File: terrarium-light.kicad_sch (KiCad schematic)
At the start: 37 parts, among them J1 USB_C_Receptacle_USB2.0_14P, Q1 UMH3N, U1 CH340C, U2 AL8860WT, U3 AL8860WT

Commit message: updates
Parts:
- removed C1, C2: C, symbol Device:C
- removed D13, D14: LED, symbol Device:LED
- removed D25, D26: D, symbol Device:D
- removed L1, L2: L, symbol Device:L
- removed R1, R2: R, symbol Device:R
- removed U2, U3: AL8860WT, Package_TO_SOT_SMD:TSOT-23-5, symbol Driver_LED:AL8860WT
- added C1, C3: C in, symbol Device:C_Small
- added C2, C4: C out, symbol Device:C_Small
- added D13, D14: D_Schottky, symbol Device:D_Schottky
- added D25, D26: LED, symbol Device:LED
- added L1, L2: L_Iron, symbol Device:L_Iron
- added R1, R2: Rset, symbol Device:R_Small
- added U2, U3: TPS61169DCKR, DCK0005A_N, symbol TPS61169DCKR:TPS61169DCKR
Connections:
- net +5V: now also C1.1, C3.1, L1.1, L2.1, U2.5 (VIN), U3.5 (VIN)
- net Earth: now also C1.2, C2.2, C3.2, C4.2, R1.2, R2.2, U2.2 (GND), U3.2 (GND)
- net at D12.1 (K): now also R1.1, U2.3 (FB)
- net at D24.1 (K): now also D25.2 (A)
- net at D1.2 (A): now also C4.1, D13.1 (K)
- net at D15.2 (A): now also C2.1, D14.1 (K)
- new net: D14.2 (A), L2.2, U3.1 (SW)
- new net: D26.1 (K), R2.1, U3.3 (FB)
- new net: D25.1 (K), D26.2 (A)
- new net: D13.2 (A), L1.2, U2.1 (SW)
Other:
- moved on the sheet: D1, D10, D11, D12, D2, D3, D4, D5, D6, D7, D8, D9

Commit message: CH340C seems good
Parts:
- added C5: 0.1uF, symbol Device:C_Small
- added R3, R4: 5.1K, symbol Device:R_Small
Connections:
- net +5V: now also J1.A4 (VBUS), J1.A9 (VBUS), J1.B4 (VBUS), J1.B9 (VBUS), U1.16 (VCC)
- net GND: now also C5.1, R3.2, R4.2
- net at U1.4 (V3): now also C5.2
- net at J1.A5 (CC1): now also R3.1
- net at J1.B5 (CC2): now also R4.1
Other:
- moved on the sheet: J1, Q1A, Q1B, U1

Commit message: updates
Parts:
- added C6: 0.1uF, symbol Device:C_Small
- added C7: 1uF, symbol Device:C_Small
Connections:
- net +5V: no longer U1.16 (VCC)
- net GND: now also C5.2, C6.1, C7.2; no longer C5.1
- net ~{RTS}: no longer Q1.6 (C1)
- net +3.3V: now reaches U1.4 (V3)
- net +3.3V: now also C5.1, U1.16 (VCC), C6.2; no longer C5.2
- net IO0 renamed ESP_IO0
- net ESP_IO0: now also C7.1
- new net ESP_EN: Q1.6 (C1)
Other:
- moved on the sheet: C5, Q1A, Q1B, U1

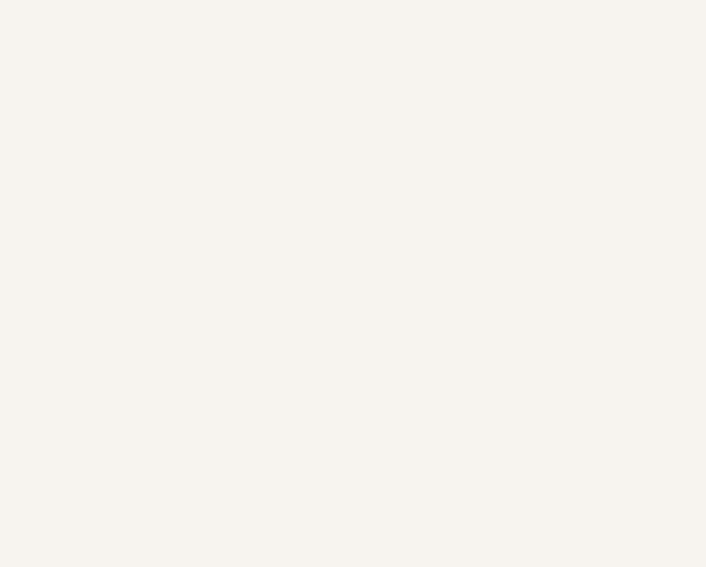
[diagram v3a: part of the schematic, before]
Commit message: what
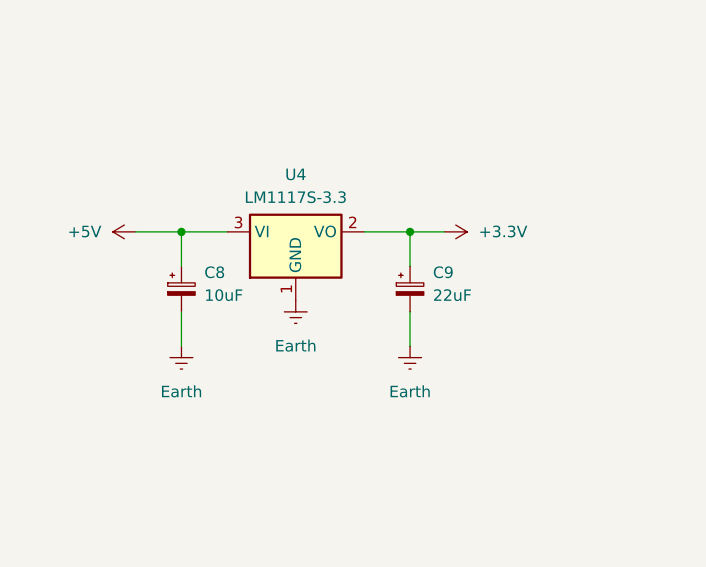
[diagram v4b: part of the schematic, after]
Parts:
- added C8: 10uF, symbol Device:C_Polarized_Small
- added C9: 22uF, symbol Device:C_Polarized_Small
- added U4: LM1117S-3.3, Package_TO_SOT_SMD:TO-263-3_TabPin2, symbol Regulator_Linear:LM1117S-3.3
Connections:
- net +3.3V: now also C9.1, U4.2 (VO)
- net +5V: now also C8.1, U4.3 (VI)
- net Earth: now also C8.2, C9.2, U4.1 (GND)

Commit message: added footprint
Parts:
- added U5: ESP32-S3-MINI-1U, RF_Module:ESP32-S2-MINI-1U, symbol MCU_Espressif:ESP32-S3-MINI-1U
- D1, D10, D11, D12, D15, D16, D17, D18, D19, D2, D20, D21, D22, D23, D24, D25, D26, D3, D4, D5, D6, D7, D8, D9: footprint (none) -> LED_SMD:LED_SPMWHD32AMH0XAR0PR
- J1: footprint (none) -> Connector_USB:USB_C_Receptacle_GCT_USB4105-xx-A_16P_TopMnt_Horizontal
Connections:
- new net: U5.1 (GND), U5.2 (GND), U5.42 (GND), U5.43 (GND), U5.46 (GND), U5.47 (GND), U5.48 (GND), U5.49 (GND), U5.50 (GND), U5.51 (GND), U5.52 (GND), U5.53 (GND), U5.54 (GND), U5.55 (GND), U5.56 (GND), U5.57 (GND), U5.58 (GND), U5.59 (GND), U5.60 (GND), U5.61 (GND), U5.62 (GND), U5.63 (GND), U5.64 (GND), U5.65 (GND)

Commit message: tried to add some stuff
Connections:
- net +3.3V: now also U5.3 (3V3)
- net ESP_EN: now also U5.45 (EN)
- net ESP_IO0: now also U5.4 (IO0)
- net GND: now also U5.1 (GND), U5.2 (GND), U5.42 (GND), U5.43 (GND), U5.46 (GND), U5.47 (GND), U5.48 (GND), U5.49 (GND), U5.50 (GND), U5.51 (GND), U5.52 (GND), U5.53 (GND), U5.54 (GND), U5.55 (GND), U5.56 (GND), U5.57 (GND), U5.58 (GND), U5.59 (GND), U5.60 (GND), U5.61 (GND), U5.62 (GND), U5.63 (GND), U5.64 (GND), U5.65 (GND)
- net ESP_32_RX: now reaches U1.2 (TXD)
- net ESP_32_RX: now also U5.40 (RXD0)
- net ESP_32_TX: now reaches U1.3 (RXD)
- net ESP_32_TX: now also U5.39 (TXD0)
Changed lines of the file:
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@@
 	(wire
 		(pts
+			(xy 30.48 59.69) (xy 40.64 59.69)
+		)
+		(stroke
+			(width 0)
+			(type default)
+		)
+	)
+	(wire
+		(pts
 			(xy 52.07 232.41) (xy 60.96 232.41)
 		)
@@
 	(wire
 		(pts
-			(xy 115.57 229.87) (xy 124.46 229.87)
+			(xy 115.57 229.87) (xy 135.89 229.87)
+		)
+		(stroke
+			(width 0)
+			(type default)
+		)
+	)
+	(wire
+		(pts
+			(xy 30.48 54.61) (xy 40.64 54.61)
 		)
 		(stroke
@@
 		)
 	)
+	(label "ESP_32_TX"
+		(at 71.12 54.61 0)
+		(fields_autoplaced yes)
+		(effects
+			(font
+				(size 1.27 1.27)
+			)
+			(justify left bottom)
+		)
+	)
 	(label "~{DTR}"
 		(at 148.59 231.14 0)
@@
 		)
 	)
+	(label "ESP_32_TX"
+		(at 120.65 238.76 0)
+		(fields_autoplaced yes)
+		(effects
+			(font
+				(size 1.27 1.27)
+			)
+			(justify left bottom)
+		)
+	)
+	(label "ESP_32_RX"
+		(at 120.65 236.22 0)
+		(fields_autoplaced yes)
+		(effects
+			(font
+				(size 1.27 1.27)
+			)
+			(justify left bottom)
+		)
+	)
 	(label "ESP_EN"
 		(at 163.83 226.06 0)
@@
 		)
 	)
+	(label "ESP_EN"
+		(at 30.48 54.61 0)
+		(fields_autoplaced yes)
+		(effects
+			(font
+				(size 1.27 1.27)
+			)
+			(justify left bottom)
+		)
+	)
 	(label "D-"
 		(at 96.52 246.38 0)
@@
 		)
 	)
+	(label "ESP_32_RX"
+		(at 71.12 57.15 0)
+		(fields_autoplaced yes)
+		(effects
+			(font
+				(size 1.27 1.27)
+			)
+			(justify left bottom)
+		)
+	)
+	(label "ESP_IO0"
+		(at 30.48 59.69 0)
+		(fields_autoplaced yes)
+		(effects
+			(font
+				(size 1.27 1.27)
+			)
+			(justify left bottom)
+		)
+	)
 	(symbol
 		(lib_id "Device:LED")
@@
 	)
 	(symbol
+		(lib_id "power:GND")
+		(at 55.88 110.49 0)
+		(unit 1)
+		(exclude_from_sim no)
+		(in_bom yes)
+		(on_board yes)
+		(dnp no)
+		(fields_autoplaced yes)
+		(property "Reference" "#PWR026"
+			(at 55.88 116.84 0)
+			(effects
+				(font
+					(size 1.27 1.27)
+				)
+				(hide yes)
+			)
+		)
+		(property "Value" "GND"
+			(at 55.88 115.57 0)
+			(effects
+				(font
+					(size 1.27 1.27)
+				)
+			)
+		)
+		(property "Footprint" ""
+			(at 55.88 110.49 0)
+			(effects
+				(font
+					(size 1.27 1.27)
+				)
+				(hide yes)
+			)
+		)
+		(property "Datasheet" ""
+			(at 55.88 110.49 0)
+			(effects
+				(font
+					(size 1.27 1.27)
+				)
+				(hide yes)
+			)
+		)
+		(property "Description" "Power symbol creates a global label with name \"GND\" , ground"
+			(at 55.88 110.49 0)
+			(effects
+				(font
+					(size 1.27 1.27)
+				)
+				(hide yes)
+			)
+		)
+		(pin "1"
+		)
+		(instances
+			(project "terrarium-light"
+				(path "/15920752-a750-4c65-817e-4525ac22cfdb"
+					(reference "#PWR026")
+					(unit 1)
+				)
+			)
+		)
+	)
+	(symbol
 		(lib_id "power:Earth")
 		(at 228.6 129.54 0)
@@
 	(symbol
 		(lib_id "power:GND")
-		(at 124.46 229.87 0)
+		(at 135.89 229.87 0)
 		(unit 1)
 		(exclude_from_sim no)
@@
 		(fields_autoplaced yes)
 		(property "Reference" "#PWR02"
-			(at 124.46 236.22 0)
+			(at 135.89 236.22 0)
 			(effects
 				(font
@@
 		)
 		(property "Value" "GND"
-			(at 124.46 234.95 0)
+			(at 135.89 234.95 0)
 			(effects
 				(font
@@
 		)
 		(property "Footprint" ""
-			(at 124.46 229.87 0)
+			(at 135.89 229.87 0)
 			(effects
 				(font
@@
 		)
 		(property "Datasheet" ""
-			(at 124.46 229.87 0)
+			(at 135.89 229.87 0)
 			(effects
 				(font
@@
 		)
 		(property "Description" "Power symbol creates a global label with name \"GND\" , ground"
-			(at 124.46 229.87 0)
+			(at 135.89 229.87 0)
 			(effects
 				(font
@@
 					(unit 1)
 				)
+			)
+		)
+	)
+	(symbol
+		(lib_id "power:+3.3V")
+		(at 55.88 49.53 0)
+		(unit 1)
+		(exclude_from_sim no)
+		(in_bom yes)
+		(on_board yes)
+		(dnp no)
+		(fields_autoplaced yes)
+		(property "Reference" "#PWR025"
+			(at 55.88 53.34 0)
+			(effects
+				(font
+					(size 1.27 1.27)
+				)
+				(hide yes)
+			)
+		)
+		(property "Value" "+3.3V"
+			(at 55.88 44.45 0)
+			(effects
+				(font
+					(size 1.27 1.27)
+				)
+			)
+		)
+		(property "Footprint" ""
+			(at 55.88 49.53 0)
+			(effects
+				(font
+					(size 1.27 1.27)
+				)
+				(hide yes)
+			)
+		)
+		(property "Datasheet" ""
+			(at 55.88 49.53 0)
+			(effects
+				(font
+					(size 1.27 1.27)
+				)
+				(hide yes)
+			)
+		)
+		(property "Description" "Power symbol creates a global label with name \"+3.3V\""
+			(at 55.88 49.53 0)
+			(effects
+				(font
+					(size 1.27 1.27)
+				)
+				(hide yes)
+			)
+		)
+		(pin "1"
+		)
+		(instances
+			(project "terrarium-light"
+				(path "/15920752-a750-4c65-817e-4525ac22cfdb"
+					(reference "#PWR025")
+					(unit 1)
+				)

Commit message: done
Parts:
- added C10: 10uf, symbol Device:C_Small
- added C11: C_Polarized_Small, symbol Device:C_Polarized_Small
- added FB1: FerriteBead_Small, symbol Device:FerriteBead_Small
- added SW1: RotaryEncoder, symbol Device:RotaryEncoder

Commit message: added parts
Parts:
- removed C8: 10uF, symbol Device:C_Polarized_Small
- added C8: 10uf, symbol Device:C_Small
- C1, C3: value C in -> 4.7uF; footprint (none) -> Capacitor_SMD:C_0805_2012Metric_Pad1.18x1.45mm_HandSolder
- C2, C4: value C out -> 4.7uF; footprint (none) -> Capacitor_SMD:C_0805_2012Metric_Pad1.18x1.45mm_HandSolder
- C9: symbol Device:C_Polarized_Small -> Device:C_Small
- D13, D14: value D_Schottky -> SK16; footprint (none) -> Diode_SMD:D_SMA_Handsoldering
- L1, L2: value L_Iron -> VLS6045EX-100M-H; footprint (none) -> Inductor_SMD:L_TDK_VLS6045EX_VLS6045AF
- R1, R2: value Rset -> 2.04ohm; footprint (none) -> Resistor_SMD:R_0805_2012Metric_Pad1.20x1.40mm_HandSolder
- U2, U3: footprint DCK0005A_N -> Package_TO_SOT_SMD:SOT-353_SC-70-5_Handsoldering
- U5: footprint RF_Module:ESP32-S2-MINI-1U -> (none)
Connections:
- net Earth is gone; now on net GND: C1.2, C2.2, C3.2, C4.2, C9.2, J1.S1 (SHIELD), R1.2, R2.2, U2.2 (GND), U3.2 (GND), U4.1 (GND)
- net +5V: now also C8.1
- net GND: now also C8.2
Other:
- note added: "4.7uF GRT21BR61H475ME13L"
